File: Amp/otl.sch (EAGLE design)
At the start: 59 parts, among them X1 MOUNT-PAD2.0, X10 MOUNT-PAD2.0, X11 MOUNT-PAD2.0, X2 MOUNT-PAD2.0, X3 MOUNT-PAD2.0, X4 MOUNT-PAD2.0, X5 MOUNT-PAD2.0, X6 MOUNT-PAD2.0, X7 MOUNT-PAD2.0, X8 MOUNT-PAD2.0, X9 MOUNT-PAD2.0

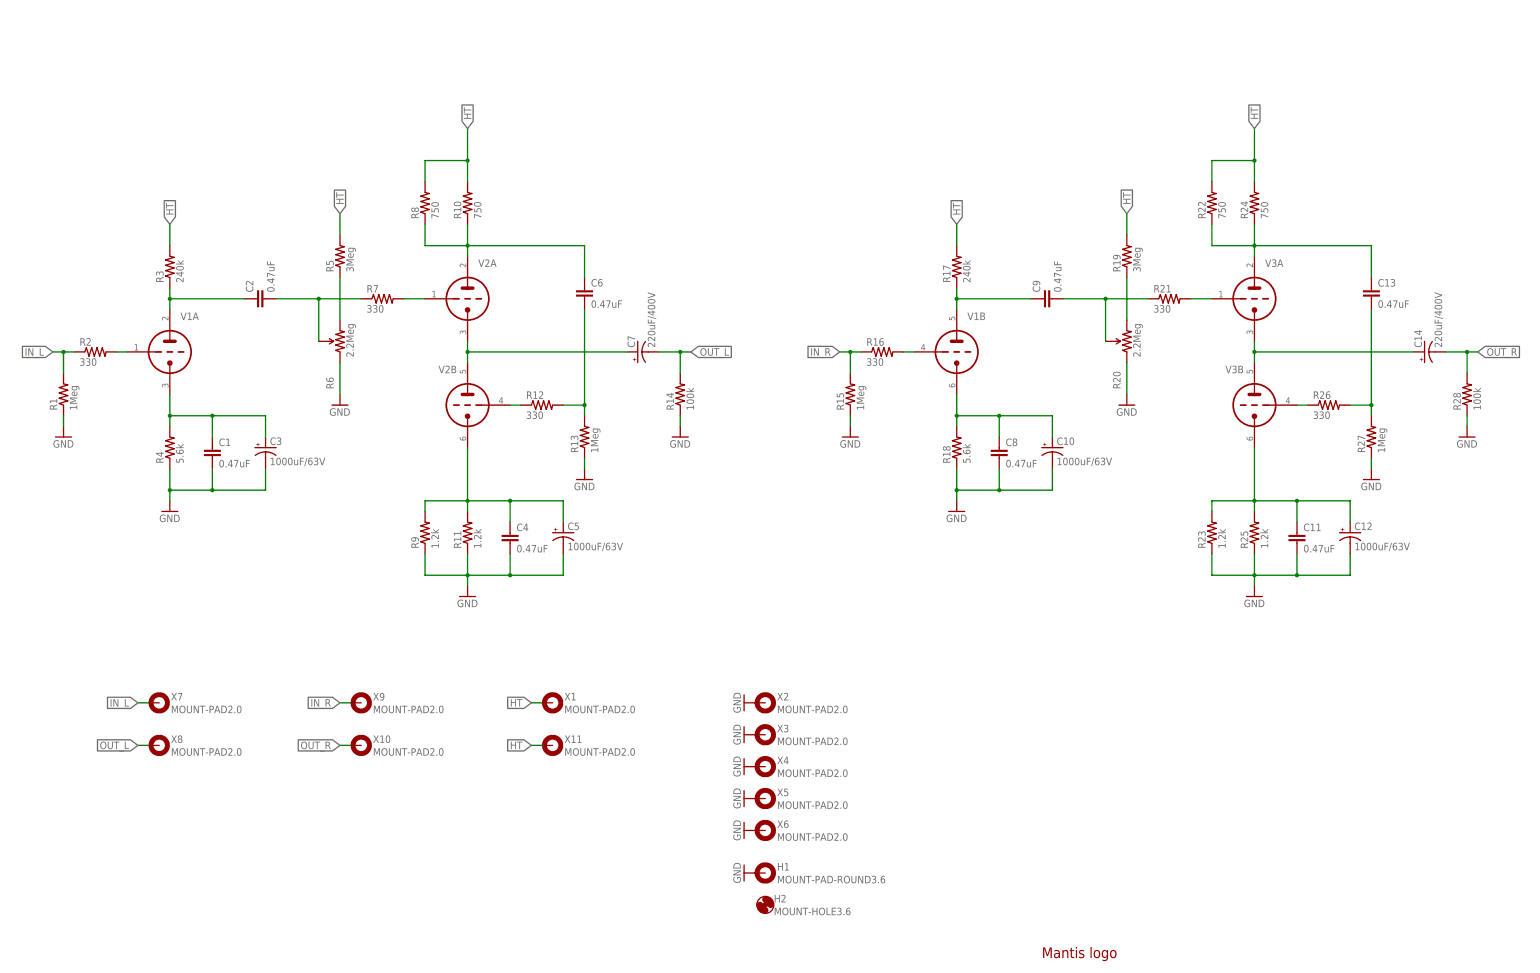
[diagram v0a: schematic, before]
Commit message: Power buses separated
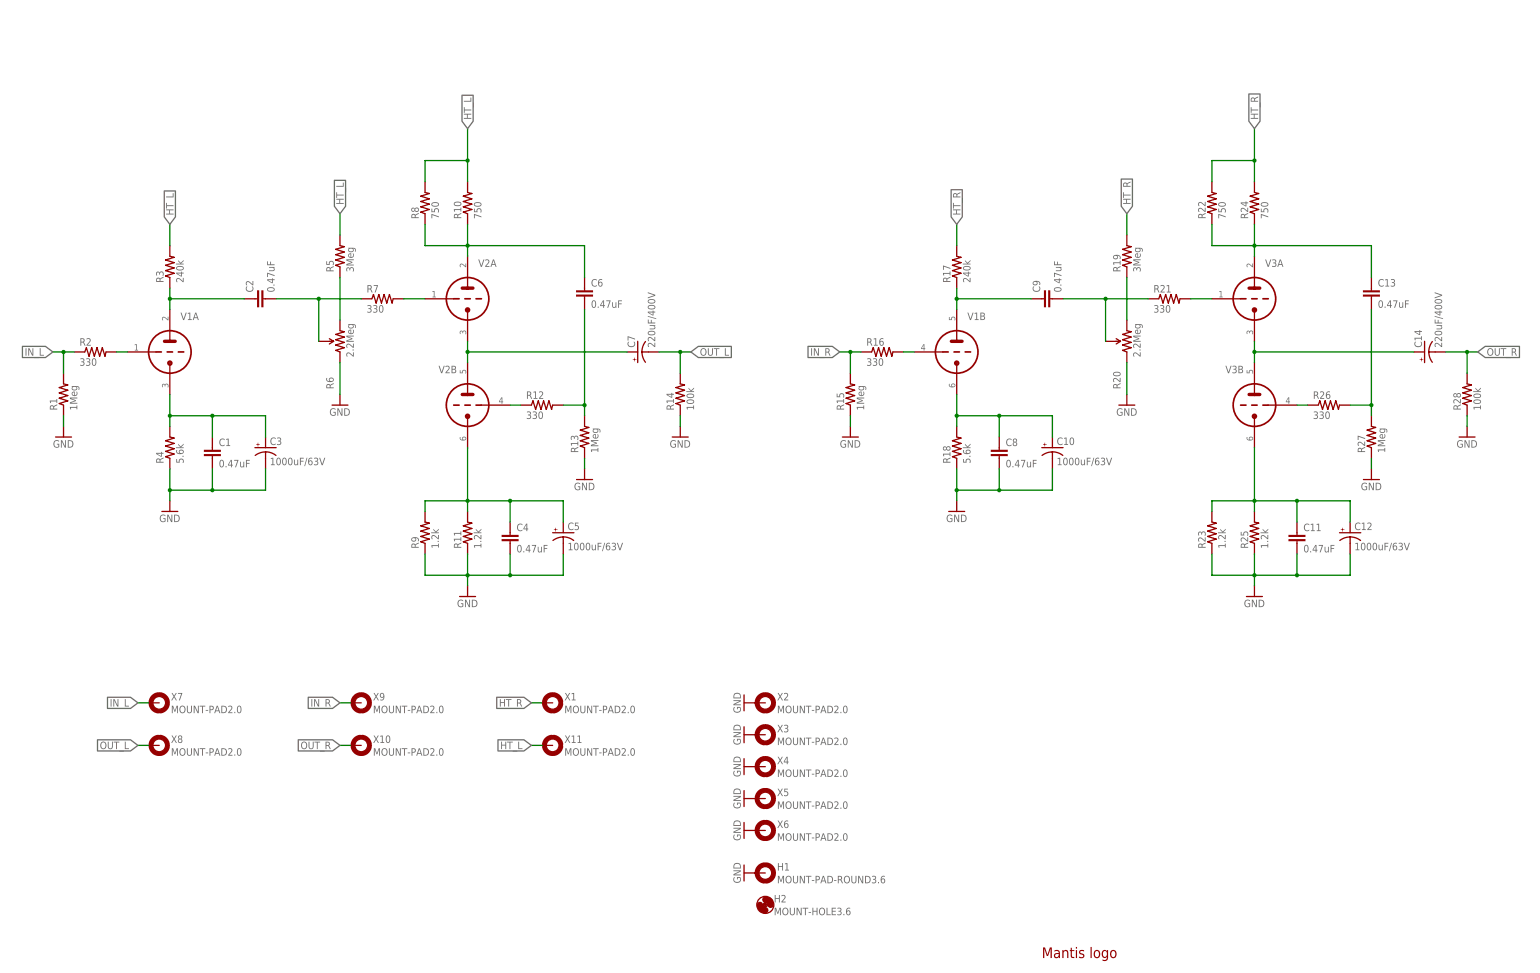
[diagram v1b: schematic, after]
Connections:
- removed net HT: R10.2, R17.2, R19.2, R22.2, R24.2, R3.2, R5.2, R8.2, X1.MOUNT, X11.MOUNT
- new net HT_L: R10.2, R3.2, R5.2, R8.2, X11.MOUNT
- new net HT_R: R17.2, R19.2, R22.2, R24.2, X1.MOUNT

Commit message: Made direct coupled
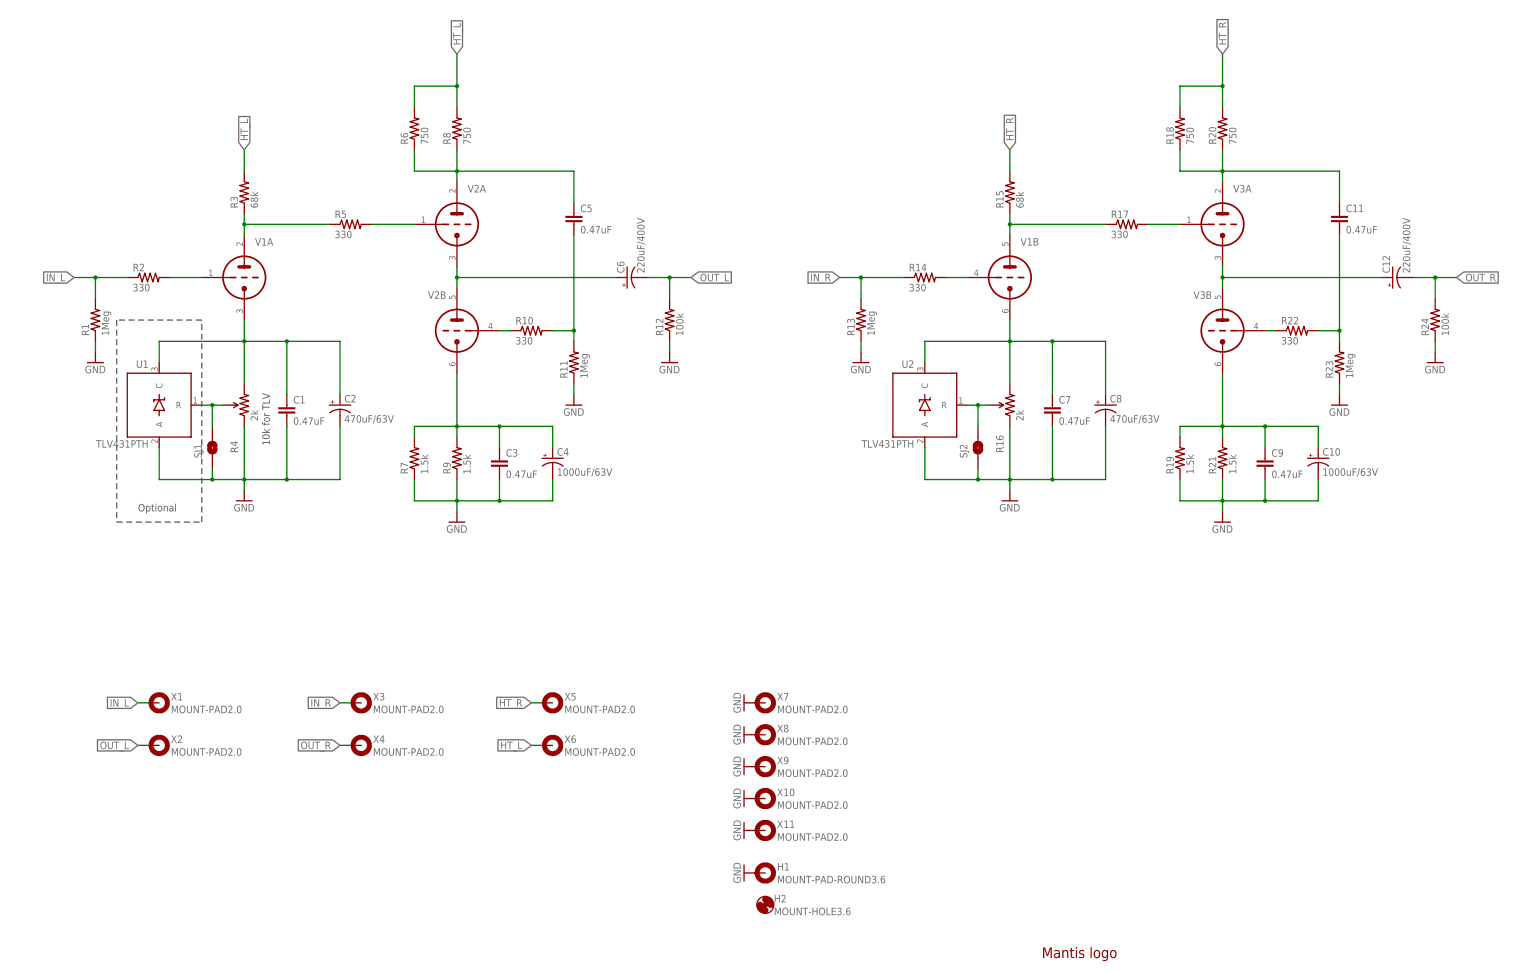
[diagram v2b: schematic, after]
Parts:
- removed C13: 0.47uF, capacitor-wima:C22/11
- removed C14: 220uF/400V, my-cap:CAP_POLPTH-25/12.5
- removed R25: 1.2k, my-res:RESISTORPTH-2W
- removed R26: 330, my-res:RESISTORPTH-1/4W
- removed R27: 1Meg, my-res:RESISTORPTH-1/4W
- removed R28: 100k, my-res:RESISTORPTH-1/4W
- added SJ1, SJ2: SOLDERJUMPERNO-LARGE, my-conn:SOLDERJUMPERNO-LARGE
- added U1, U2: TLV431PTH, my-reg:TLV431PTH
- C11: device capacitor-wima:C5/5.5 -> capacitor-wima:C22/11
- C12: value 1000uF/63V -> 220uF/400V; device my-cap:CAP_POLPTH-16/7.5 -> my-cap:CAP_POLPTH-25/12.5
- C2: value 0.47uF -> 470uF/63V; device capacitor-wima:C22/11 -> my-cap:CAP_POLPTH-16/7.5
- C3: value 1000uF/63V -> 0.47uF; device my-cap:CAP_POLPTH-16/7.5 -> capacitor-wima:C5/5.5
- C4: value 0.47uF -> 1000uF/63V; device capacitor-wima:C5/5.5 -> my-cap:CAP_POLPTH-16/7.5
- C5: value 1000uF/63V -> 0.47uF; device my-cap:CAP_POLPTH-16/7.5 -> capacitor-wima:C22/11
- C6: value 0.47uF -> 220uF/400V; device capacitor-wima:C22/11 -> my-cap:CAP_POLPTH-25/12.5
- C7: value 220uF/400V -> 0.47uF; device my-cap:CAP_POLPTH-25/12.5 -> capacitor-wima:C5/5.5
- C8: value 0.47uF -> 470uF/63V; device capacitor-wima:C5/5.5 -> my-cap:CAP_POLPTH-16/7.5
- C9: device capacitor-wima:C22/11 -> capacitor-wima:C5/5.5
- R10, R22: value 750 -> 330; device my-res:RESISTORPTH-2W -> my-res:RESISTORPTH-1/4W
- R11, R23: value 1.2k -> 1Meg; device my-res:RESISTORPTH-2W -> my-res:RESISTORPTH-1/4W
- R12: value 330 -> 100k
- R14: value 100k -> 330
- R15: value 1Meg -> 68k; device my-res:RESISTORPTH-1/4W -> my-res:RESISTORPTH-2W
- R16: value 330 -> 2k; device my-res:RESISTORPTH-1/4W -> SparkFun-Electromechanical:TRIMPOT3362U-2
- R17: value 240k -> 330
- R18: value 5.6k -> 750; device my-res:RESISTORPTH-1/4W -> my-res:RESISTORPTH-2W
- R19: value 3Meg -> 1.5k; device my-res:RESISTORPTH-1/4W -> my-res:RESISTORPTH-2W
- R20, R6: value 2.2Meg -> 750; device SparkFun-Electromechanical:TRIMPOT3362U-2 -> my-res:RESISTORPTH-2W
- R21, R7: value 330 -> 1.5k; device my-res:RESISTORPTH-1/4W -> my-res:RESISTORPTH-2W
- R24: value 750 -> 100k; device my-res:RESISTORPTH-2W -> my-res:RESISTORPTH-1/4W
- R3: value 240k -> 68k; device my-res:RESISTORPTH-1/4W -> my-res:RESISTORPTH-2W
- R4: value 5.6k -> 2k; device my-res:RESISTORPTH-1/4W -> SparkFun-Electromechanical:TRIMPOT3362U-2
- R5: value 3Meg -> 330
- R9: value 1.2k -> 1.5k
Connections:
- removed net N$22: C9.2, R20.WIPER, R21.1
- removed net N$7: R5.1, R6.CW
- net GND: now also C2.-, C3.2, C4.-, C7.2, C8.-, C9.2, R12.1, R16.CCW, R19.1, R21.1, R24.1, R4.CCW, R7.1, SJ1.1, SJ2.1, U1.A, U2.A, X10.MOUNT, X11.MOUNT, X7.MOUNT, X8.MOUNT, X9.MOUNT; no longer C11.2, C12.-, C3.-, C4.2, C5.-, C8.2, R14.1, R15.1, R18.1, R20.CCW, R25.1, R27.1, R28.1, R4.1, R6.CCW, X2.MOUNT, X3.MOUNT, X4.MOUNT, X5.MOUNT, X6.MOUNT
- net HT_L: now also R6.2, X6.MOUNT; no longer R10.2, R5.2, X11.MOUNT
- net HT_R: now also R15.2, R18.2, R20.2, X5.MOUNT; no longer R17.2, R19.2, R22.2, R24.2, X1.MOUNT
- net IN_L: now also X1.MOUNT; no longer X7.MOUNT
- net IN_R: now also R13.2, R14.1, X3.MOUNT; no longer R15.2, R16.1, X9.MOUNT
- net N$1: now also C5.1, R6.1; no longer C6.1, R10.1
- net N$10: now also R22.1; no longer R26.1
- net N$11: now also C6.+; no longer C7.+
- net N$12: now also C10.+, C9.1, R19.2, R21.2; no longer C11.1, C12.+, R23.2, R25.2
- net N$13: now also C11.2, R22.2, R23.2; no longer C13.2, R26.2, R27.2
- net N$14: now also R17.2; no longer R21.2
- net N$15: now also R16.WIPER, SJ2.2, U2.R; no longer R19.1, R20.CW
- net N$16: now also C7.1, C8.+, R16.CW, U2.C; no longer C10.+, C8.1, R18.2
- net N$17: now also R15.1; no longer C9.1
- net N$18: now also C12.+; no longer C14.+
- net N$2: now also C11.1, R18.1, R20.1; no longer C13.1, R22.1, R24.1
- net N$20: now also R4.WIPER, SJ1.2, U1.R; no longer C2.2, R6.WIPER, R7.1
- net N$21: now also R14.2; no longer R16.2
- net N$3: now also R10.1; no longer R12.1
- net N$4: now also C2.+, R4.CW, U1.C; no longer C3.+, R4.2
- net N$5: now also C3.1, C4.+, R7.2; no longer C4.1, C5.+, R11.2
- net N$6: now also C5.2, R10.2, R11.2; no longer C6.2, R12.2, R13.2
- net N$8: now also R5.2; no longer R7.2
- net N$9: now also R5.1; no longer C2.1
- net OUT_L: now also C6.-, R12.2, X2.MOUNT; no longer C7.-, R14.2, X8.MOUNT
- net OUT_R: now also C12.-, R24.2, X4.MOUNT; no longer C14.-, R28.2, X10.MOUNT
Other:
- note added: "10k for TLV"
- note added: "Optional"
- moved on the sheet: C1, C10, C11, C12, C9, R1, R10, R11, R12, R13, R14, R15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

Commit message: Tubes' names added
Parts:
- V1: value (none) -> 6SN7-GTB
- V2, V3: value (none) -> 6AS7-G
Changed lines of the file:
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@@
 </classes>
 <parts>
-<part name="V2" library="my-tubes" deviceset="6AS7G-P-NH" device="OUTLET"/>
+<part name="V2" library="my-tubes" deviceset="6AS7G-P-NH" device="OUTLET" value="6AS7-G"/>
 <part name="R6" library="my-res" deviceset="RESISTOR" device="PTH-2W" value="750"/>
 <part name="R8" library="my-res" deviceset="RESISTOR" device="PTH-2W" value="750"/>
@@
 <part name="R5" library="my-res" deviceset="RESISTOR" device="PTH-1/4W" value="330"/>
 <part name="FRAME1" library="frames" deviceset="DINA3_L" device=""/>
-<part name="V1" library="my-tubes" deviceset="6SN7GT-P-NH" device="OUTLET"/>
+<part name="V1" library="my-tubes" deviceset="6SN7GT-P-NH" device="OUTLET" value="6SN7-GTB"/>
 <part name="C1" library="capacitor-wima" deviceset="C" device="5/5.5" value="0.47uF"/>
 <part name="C2" library="my-cap" deviceset="CAP_POL" device="PTH-16/7.5" value="470uF/63V"/>
@@
 <part name="R12" library="my-res" deviceset="RESISTOR" device="PTH-1/4W" value="100k"/>
 <part name="GND5" library="SparkFun-Aesthetics" deviceset="GND" device=""/>
-<part name="V3" library="my-tubes" deviceset="6AS7G-P-NH" device="OUTLET"/>
+<part name="V3" library="my-tubes" deviceset="6AS7G-P-NH" device="OUTLET" value="6AS7-G"/>
 <part name="R18" library="my-res" deviceset="RESISTOR" device="PTH-2W" value="750"/>
 <part name="R20" library="my-res" deviceset="RESISTOR" device="PTH-2W" value="750"/>
